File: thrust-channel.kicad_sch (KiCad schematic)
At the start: 4 parts, among them Q22 2SD1834T100, U40 LM324, U42 MAX4210EEUA+

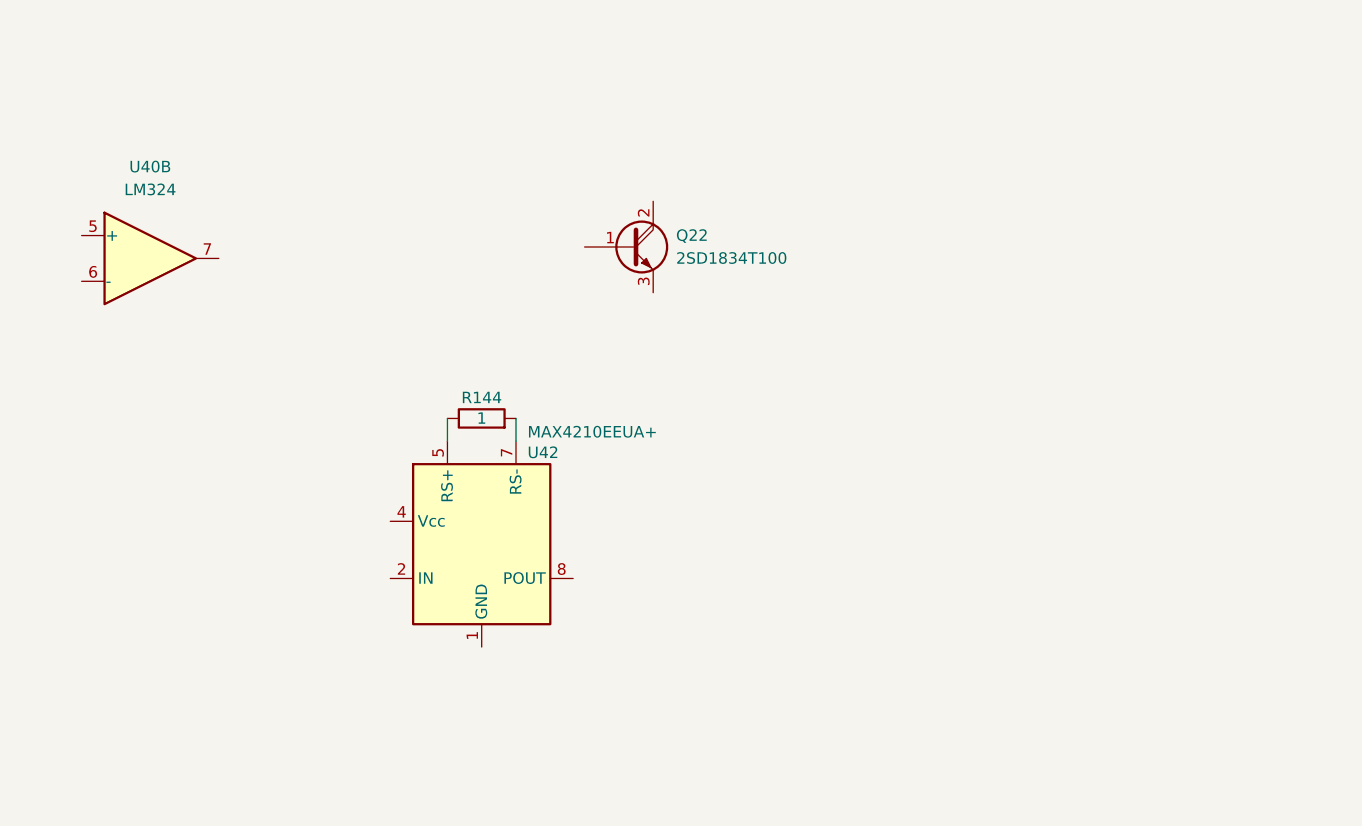
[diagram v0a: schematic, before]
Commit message: convert thrust control
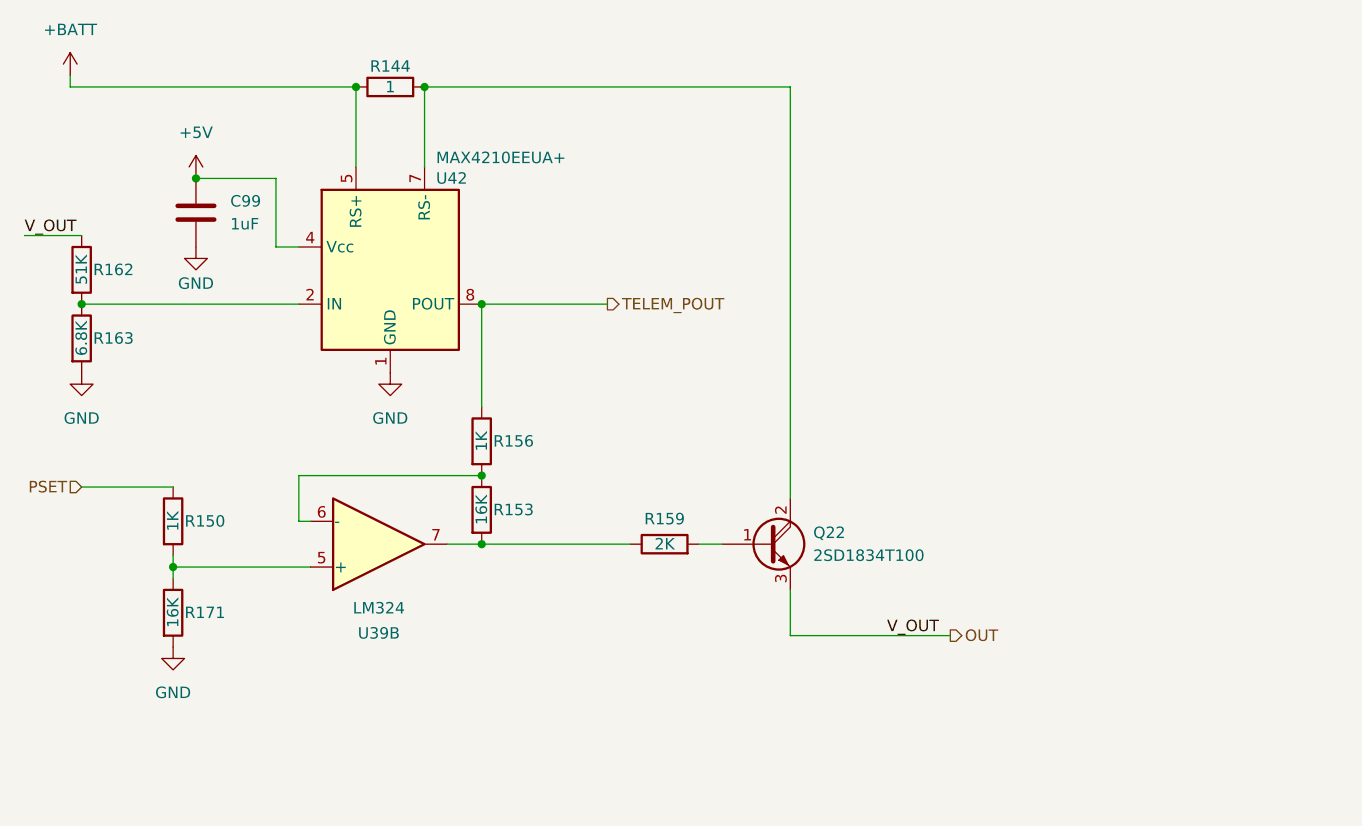
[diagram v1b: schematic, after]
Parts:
- added C99: 1uF, symbol Device:C
- added R150, R156: 1K, symbol Device:R
- added R153, R171: 16K, symbol Device:R
- added R159: 2K, symbol Device:R
- added R162: 51K, symbol Device:R
- added R163: 6.8K, symbol Device:R
- renumbered U40 to U39
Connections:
- net at U39.5 (+): now also R150.2, R171.1
- net at U39.6 (-): now also R153.1, R156.2
- net at U39.7: now also R153.2, R159.1
- net GND: now reaches U42.1 (GND)
- net GND: now also C99.2, R163.2, R171.2
- net at U42.2 (IN): now also R162.2, R163.1
- net +5V: now reaches U42.4 (Vcc)
- net +5V: now also C99.1
- net +BATT: now reaches R144.1, U42.5 (RS+)
- net at R144.2, U42.7 (RS-): now also Q22.2 (C)
- net TELEM_POUT: now reaches U42.8 (POUT)
- net TELEM_POUT: now also R156.1
- net at Q22.1 (B): now also R159.2
- net OUT: now reaches Q22.3 (E)
- net OUT: now also R162.1
- new net PSET: R150.1
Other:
- moved on the sheet: Q22, R144, U39B, U42

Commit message: work
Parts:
- renumbered C99 to C87, Q22 to Q19, R162 to R137, R163 to R138, R150 to R139, R144 to R141, R156 to R142, R153 to R143, R159 to R144, R171 to R164, U39 to U33, U42 to U36

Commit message: work
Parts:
- U36: value MAX4210EEUA+ -> MAX4210DEUA+
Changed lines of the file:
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@@
 			)
 		)
-		(property "Value" "MAX4210EEUA+"
+		(property "Value" "MAX4210DEUA+"
 			(at 96.52 47.244 0)
 			(do_not_autoplace yes)

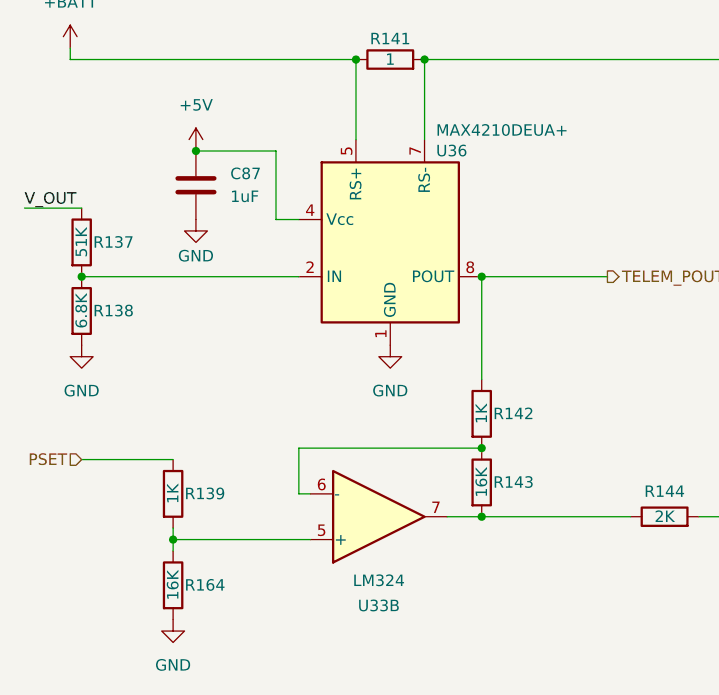
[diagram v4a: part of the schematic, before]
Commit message: thrust control
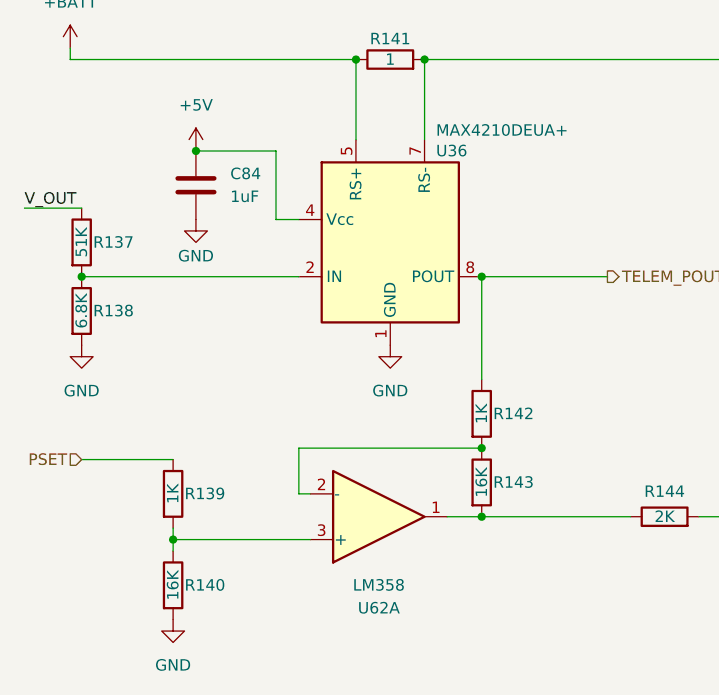
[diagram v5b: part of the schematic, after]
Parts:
- removed U33: LM324, symbol Amplifier_Operational:LM324
- added U62: LM358, symbol Amplifier_Operational:LM358
- renumbered C87 to C84, R164 to R140
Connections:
- net at R142.2, R143.1: now also U62.2 (-)
- net at R143.2, R144.1: now also U62.1
- net at R139.2, R140.1: now also U62.3 (+)

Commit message: work
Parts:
- added U84: FEMTA, symbol femta-control-custom:FEMTA
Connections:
- net GND: now also U84.2 (V-)
- net OUT renamed V_OUT
- net V_OUT: now also U84.1 (V+)
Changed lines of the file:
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@@
+	)
+	(junction
+		(at 135.89 100.33)
+		(diameter 0)
+		(color 0 0 0 0)
 	)
 	(junction
@@
 	(wire
 		(pts
-			(xy 135.89 100.33) (xy 153.67 100.33)
+			(xy 135.89 100.33) (xy 143.51 100.33)
 		)
 		(stroke
@@
 	)
 	(label "V_OUT"
-		(at 152.4 100.33 180)
+		(at 143.51 100.33 180)
 		(fields_autoplaced yes)
 		(effects
@@
 		(shape output)
 		(at 115.57 63.5 0)
-		(fields_autoplaced yes)
-		(effects
-			(font
-				(size 1.27 1.27)
-			)
-			(justify left)
-		)
-	)
-	(hierarchical_label "OUT"
-		(shape output)
-		(at 153.67 100.33 0)
 		(fields_autoplaced yes)
 		(effects
@@
 	)
 	(symbol
+		(lib_id "femta-control-custom:FEMTA")
+		(at 138.43 106.68 270)
+		(unit 1)
+		(exclude_from_sim no)
+		(in_bom yes)
+		(on_board yes)
+		(dnp no)
+		(fields_autoplaced yes)
+		(property "Reference" "U84"
+			(at 139.7 105.4099 90)
+			(effects
+				(font
+					(size 1.27 1.27)
+				)
+				(justify left)
+			)
+		)
+		(property "Value" "FEMTA"
+			(at 139.7 107.9499 90)
+			(effects
+				(font
+					(size 1.27 1.27)
+				)
+				(justify left)
+			)
+		)
+		(property "Footprint" ""
+			(at 138.43 106.68 0)
+			(effects
+				(font
+					(size 1.27 1.27)
+				)
+				(hide yes)
+			)
+		)
+		(property "Datasheet" ""
+			(at 138.43 106.68 0)
+			(effects
+				(font
+					(size 1.27 1.27)
+				)
+				(hide yes)
+			)
+		)
+		(property "Description" ""
+			(at 138.43 106.68 0)
+			(effects
+				(font
+					(size 1.27 1.27)
+				)
+				(hide yes)
+			)
+		)
+		(pin "1"
+		)
+		(pin "2"
+		)
+		(instances
+			(project "femta-control"
+				(path "/838bf11c-36b7-41d7-9462-fe98a188d617/3bf849ef-bca6-4864-a347-fbff558d0891/49dafe5d-519c-49b1-88d9-ec8cb6df7648"
+					(reference "U84")
+					(unit 1)
+				)
+				(path "/838bf11c-36b7-41d7-9462-fe98a188d617/c8752098-45e2-4d20-a718-e7a412b889c5/193305be-6cda-4233-81aa-0afa66e3e4ce"
+					(reference "U80")
+					(unit 1)
+				)
+				(path "/838bf11c-36b7-41d7-9462-fe98a188d617/c8752098-45e2-4d20-a718-e7a412b889c5/f663376f-9b89-41b3-aeca-9c6d61fe2c6e"
+					(reference "U81")
+					(unit 1)
+				)
+				(path "/838bf11c-36b7-41d7-9462-fe98a188d617/25504b25-63a2-43d8-9fee-c553eccedd0e/193305be-6cda-4233-81aa-0afa66e3e4ce"
+					(reference "U82")
+					(unit 1)
+				)
+				(path "/838bf11c-36b7-41d7-9462-fe98a188d617/25504b25-63a2-43d8-9fee-c553eccedd0e/f663376f-9b89-41b3-aeca-9c6d61fe2c6e"
+					(reference "U83")
+					(unit 1)
+				)
+				(path "/838bf11c-36b7-41d7-9462-fe98a188d617/3bf849ef-bca6-4864-a347-fbff558d0891/a6f30b1f-5689-4abf-92ce-ea5546b50948"
+					(reference "U85")
+					(unit 1)
+				)
+				(path "/838bf11c-36b7-41d7-9462-fe98a188d617/3bf849ef-bca6-4864-a347-fbff558d0891/8de52c6a-44a2-4c3d-988b-6d07c6a566b2"
+					(reference "U86")
+					(unit 1)
+				)
+				(path "/838bf11c-36b7-41d7-9462-fe98a188d617/3bf849ef-bca6-4864-a347-fbff558d0891/826227b2-3a4f-4a87-9419-7605bb4529f5"
+					(reference "U87")
+					(unit 1)
+				)
+				(path "/838bf11c-36b7-41d7-9462-fe98a188d617/3bf849ef-bca6-4864-a347-fbff558d0891/47cd1a1a-1480-4eae-b9ce-a73cac0b3bdc"
+					(reference "U88")
+					(unit 1)
+				)
+				(path "/838bf11c-36b7-41d7-9462-fe98a188d617/3bf849ef-bca6-4864-a347-fbff558d0891/37415780-54b9-4ed3-8ab8-f09b8d9e8267"
+					(reference "U89")
+					(unit 1)
+				)
+				(path "/838bf11c-36b7-41d7-9462-fe98a188d617/3bf849ef-bca6-4864-a347-fbff558d0891/ace2e429-6c02-47f3-a5a8-ce53fd79b4bb"
+					(reference "U90")
+					(unit 1)
+				)
+				(path "/838bf11c-36b7-41d7-9462-fe98a188d617/3bf849ef-bca6-4864-a347-fbff558d0891/b15c763d-24bc-4af2-a62c-4319be075b04"
+					(reference "U91")
+					(unit 1)
+				)
+			)
+		)
+	)
+	(symbol
 		(lib_id "power:GND")
 		(at 69.85 57.15 0)
@@
 					(unit 1)
 				)
+			)
+		)
+	)
+	(symbol
+		(lib_id "power:GND")
+		(at 135.89 113.03 0)
+		(unit 1)
+		(exclude_from_sim no)
+		(in_bom yes)
+		(on_board yes)
+		(dnp no)
+		(fields_autoplaced yes)
+		(property "Reference" "#PWR0303"
+			(at 135.89 119.38 0)
+			(effects
+				(font
+					(size 1.27 1.27)
+				)
+				(hide yes)
+			)
+		)
+		(property "Value" "GND"
+			(at 135.89 118.11 0)
+			(effects
+				(font
+					(size 1.27 1.27)
+				)
+			)
+		)
+		(property "Footprint" ""
+			(at 135.89 113.03 0)
+			(effects
+				(font
+					(size 1.27 1.27)
+				)
+				(hide yes)
+			)
+		)
+		(property "Datasheet" ""
+			(at 135.89 113.03 0)
+			(effects
+				(font
+					(size 1.27 1.27)
+				)
+				(hide yes)
+			)
+		)
+		(property "Description" "Power symbol creates a global label with name \"GND\" , ground"
+			(at 135.89 113.03 0)
+			(effects
+				(font
+					(size 1.27 1.27)
+				)
+				(hide yes)
+			)
+		)
+		(pin "1"
+		)
+		(instances
+			(project "femta-control"
+				(path "/838bf11c-36b7-41d7-9462-fe98a188d617/c8752098-45e2-4d20-a718-e7a412b889c5/193305be-6cda-4233-81aa-0afa66e3e4ce"
+					(reference "#PWR0303")
+					(unit 1)
+				)
+				(path "/838bf11c-36b7-41d7-9462-fe98a188d617/c8752098-45e2-4d20-a718-e7a412b889c5/f663376f-9b89-41b3-aeca-9c6d61fe2c6e"
+					(reference "#PWR0304")
+					(unit 1)
+				)
+				(path "/838bf11c-36b7-41d7-9462-fe98a188d617/25504b25-63a2-43d8-9fee-c553eccedd0e/193305be-6cda-4233-81aa-0afa66e3e4ce"
+					(reference "#PWR0305")
+					(unit 1)
+				)
+				(path "/838bf11c-36b7-41d7-9462-fe98a188d617/25504b25-63a2-43d8-9fee-c553eccedd0e/f663376f-9b89-41b3-aeca-9c6d61fe2c6e"
+					(reference "#PWR0306")
+					(unit 1)
+				)
+				(path "/838bf11c-36b7-41d7-9462-fe98a188d617/3bf849ef-bca6-4864-a347-fbff558d0891/49dafe5d-519c-49b1-88d9-ec8cb6df7648"
+					(reference "#PWR0307")
+					(unit 1)
+				)
+				(path "/838bf11c-36b7-41d7-9462-fe98a188d617/3bf849ef-bca6-4864-a347-fbff558d0891/a6f30b1f-5689-4abf-92ce-ea5546b50948"
+					(reference "#PWR0308")
+					(unit 1)
+				)
+				(path "/838bf11c-36b7-41d7-9462-fe98a188d617/3bf849ef-bca6-4864-a347-fbff558d0891/8de52c6a-44a2-4c3d-988b-6d07c6a566b2"
+					(reference "#PWR0309")
+					(unit 1)
+				)
+				(path "/838bf11c-36b7-41d7-9462-fe98a188d617/3bf849ef-bca6-4864-a347-fbff558d0891/826227b2-3a4f-4a87-9419-7605bb4529f5"
+					(reference "#PWR0310")
+					(unit 1)
+				)
+				(path "/838bf11c-36b7-41d7-9462-fe98a188d617/3bf849ef-bca6-4864-a347-fbff558d0891/47cd1a1a-1480-4eae-b9ce-a73cac0b3bdc"
+					(reference "#PWR0311")
+					(unit 1)
+				)
+				(path "/838bf11c-36b7-41d7-9462-fe98a188d617/3bf849ef-bca6-4864-a347-fbff558d0891/37415780-54b9-4ed3-8ab8-f09b8d9e8267"
+					(reference "#PWR0312")
+					(unit 1)
+				)
+				(path "/838bf11c-36b7-41d7-9462-fe98a188d617/3bf849ef-bca6-4864-a347-fbff558d0891/ace2e429-6c02-47f3-a5a8-ce53fd79b4bb"
+					(reference "#PWR0313")
+					(unit 1)
+				)
+				(path "/838bf11c-36b7-41d7-9462-fe98a188d617/3bf849ef-bca6-4864-a347-fbff558d0891/b15c763d-24bc-4af2-a62c-4319be075b04"
+					(reference "#PWR0314")
+					(unit 1)
+				)

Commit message: work
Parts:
- removed R139: 1K, symbol Device:R
- removed R140: 16K, symbol Device:R
- R137: value 51K -> 48.7K
- R138: value 6.8K -> 2.5K
- R141: value 1 -> 500m
- R143: value 16K -> 33K
- U36: value MAX4210DEUA+ -> MAX4210FEUA+
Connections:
- net PSET: now also U62.3 (+)
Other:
- moved on the sheet: Q19, R142, R143, R144, U62A, U84

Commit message: 540 COMPONENTS I AM LOSING MY MINDDDDDD
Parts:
- renumbered C84 to C32, Q19 to Q6, R137 to R34, R138 to R35, R141 to R36, R142 to R37, R143 to R38, R144 to R39, U36 to U17, U84 to U18, U62 to U38
